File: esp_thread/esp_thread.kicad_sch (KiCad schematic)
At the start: 0 parts

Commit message: PCB in progress, temperature sensor comparison
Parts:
- added U1: 113991254, Xiao ESP32-C6:MODULE_113991254, symbol Xiao ESP32-C6:113991254
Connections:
- new net +3V3: U1.12 (3V3)
- new net +5V: U1.14 (5V)
- new net GND: U1.13 (GND)

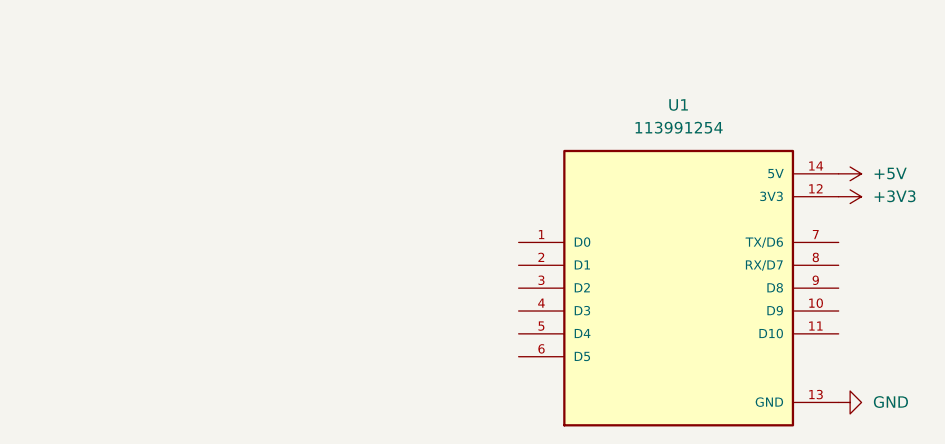
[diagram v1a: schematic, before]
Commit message: Add temperature sensor comparison script and output files, light PCB almost done, button PCB and temperature PCB in progress
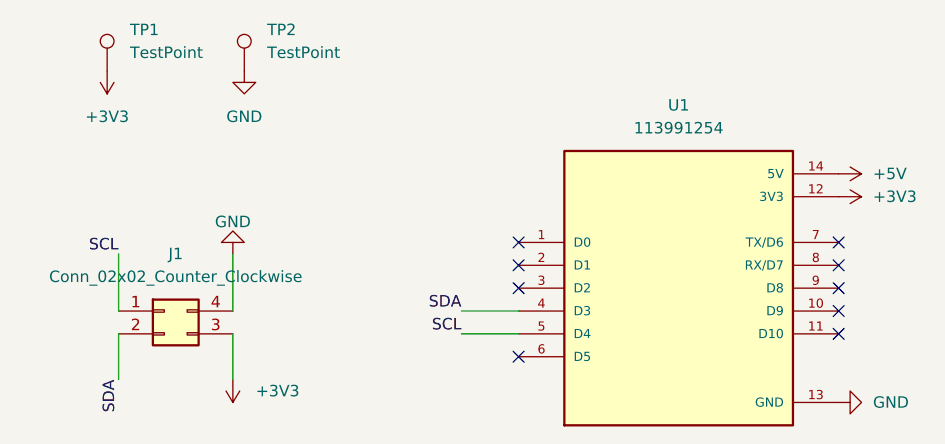
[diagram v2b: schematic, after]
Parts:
- added J1: Conn_02x02_Counter_Clockwise, Connector_PinSocket_1.27mm:PinSocket_2x02_P1.27mm_Vertical, symbol Connector_Generic:Conn_02x02_Counter_Clockwise
- added TP1, TP2: TestPoint, TestPoint:TestPoint_Pad_D1.5mm, symbol Connector:TestPoint
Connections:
- net +3V3: now also J1.3 (Pin_3), TP1.1
- net GND: now also J1.4 (Pin_4), TP2.1
- net SDA: now reaches U1.4 (D3)
- net SDA: now also J1.2 (Pin_2)
- net SCL: now reaches U1.5 (D4)
- net SCL: now also J1.1 (Pin_1)
- no-connect marks 0 -> 9
